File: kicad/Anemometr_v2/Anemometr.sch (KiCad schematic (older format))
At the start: 156 parts, among them J1 TxD, J10 +Z1, J11 +Z2, J12 +Z3, J13 +Z4, J14 -Z1, J15 -Z2, J16 -Z3, J17 -Z4, J18 1 TxD+, J19 2 TxD-, J2 RxD, J20 3 RxD+, J21 4-5, J22 6 RxD-, J23 7-8, J24 Conn_01x01_Female, J3 SCL, J4 SDA, J5 RST, J6 +EXT, J7 -EXT, J8 SWD, J9 SWC, Q1 5N10, U1 STM32F103C8Tx, U2 TS5A3166DBVR, U3 TS5A3166DBVR, U4 TS5A3166DBVR, U5 TS5A3166DBVR, U6 NCP1117-3.3, U7 MCP1703-5, U8 TLV3201DBV, U9 MCP1703-3.3, Y1 CSTCE8M00G52A-R0, Y2 QC5CB25.0000F18B23R

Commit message: изменено:      kicad/Anemometr_v2/Anemometr-cache.lib 	изменено:      kicad/Anemometr_v2/Anemometr.kicad_pcb 	изменено:      kicad/Anemometr_v2/Anemometr.kicad_pcb-bak 	изменено:      kicad/Anemometr_v2/Anemometr.sch 	изменено:      kicad/Anemometr_v2/Anemometr.sch-bak 	изменено:      kicad/Anemometr_v2/fp-info-cache 	изменено:      kicad/Anemometr_v2/gerber/Anemometr-job.gbrjob 	изменено:      kicad/Anemometr_v2/gerber/Border.gbr 	изменено:      kicad/Anemometr_v2/gerber/Bottom.gbr 	изменено:      kicad/Anemometr_v2/gerber/MaskBottom.gbr 	изменено:      kicad/Anemometr_v2/gerber/MaskTop.gbr 	изменено:      kicad/Anemometr_v2/gerber/NCData.drl 	изменено:      kicad/Anemometr_v2/gerber/Top.gbr 	изменено:      kicad/Anemometr_v2/gerber/anemometr.zip
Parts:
- removed Y2: QC5CB25.0000F18B23R, Crystal:Crystal_SMD_Qantek_QC5CB-2Pin_5x3.2mm, symbol Device:Crystal
- added J25: Conn_01x01_Female, My-library:SMD-CONN, symbol Connector:Conn_01x01_Female
- added Y2: ECS-250-20-33, Crystal:Crystal_SMD_SeikoEpson_FA238-4Pin_3.2x2.5mm, symbol Device:Crystal_GND24
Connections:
- net GND: now also Y2.2, Y2.4
- net at C47.2, R37.1, U8.3 (+): now also J25.1 (Pin_1)
- net at C7.1, D3.30 (XI), R1.1: now also Y2.3
- net at C4.1, D3.31 (XO), R1.2: now also Y2.1
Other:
- moved on the sheet: C4, C7, D1, D2, R1, R2, R3
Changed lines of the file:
@@
-$EndComp
-$Comp
-L Device:Crystal Y2
-U 1 1 61F010CD
-P 4550 8250
-F 0 "Y2" H 4200 8350 50  0000 C CNN
-F 1 "QC5CB25.0000F18B23R" H 4200 8250 50  0001 C CNN
-F 2 "Crystal:Crystal_SMD_Qantek_QC5CB-2Pin_5x3.2mm" H 4550 8250 50  0001 C CNN
-F 3 "~" H 4550 8250 50  0001 C CNN
-	1    4550 8250
-	1    0    0    -1
 $EndComp
 $Comp
 L Device:C C4
 U 1 1 61F02281
-P 4400 8400
-F 0 "C4" H 4100 8400 50  0000 L CNN
-F 1 "10p" H 4100 8300 50  0000 L CNN
-F 2 "Capacitor_SMD:C_0402_1005Metric" H 4438 8250 50  0001 C CNN
-F 3 "~" H 4400 8400 50  0001 C CNN
-	1    4400 8400
+P 4150 8600
+F 0 "C4" H 4000 8800 50  0000 L CNN
+F 1 "10p" H 4000 8700 50  0000 L CNN
+F 2 "Capacitor_SMD:C_0402_1005Metric" H 4188 8450 50  0001 C CNN
+F 3 "~" H 4150 8600 50  0001 C CNN
+	1    4150 8600
 	1    0    0    -1
 $EndComp
@@
 L Device:C C7
 U 1 1 61F03145
-P 4700 8400
-F 0 "C7" H 4700 8300 50  0000 L CNN
-F 1 "10p" H 4700 8200 50  0000 L CNN
-F 2 "Capacitor_SMD:C_0402_1005Metric" H 4738 8250 50  0001 C CNN
-F 3 "~" H 4700 8400 50  0001 C CNN
-	1    4700 8400
-	1    0    0    -1
-$EndComp
-Wire Wire Line
-	4400 8550 4550 8550
+P 4450 8600
+F 0 "C7" H 4550 8700 50  0000 L CNN
+F 1 "10p" H 4550 8600 50  0000 L CNN
+F 2 "Capacitor_SMD:C_0402_1005Metric" H 4488 8450 50  0001 C CNN
+F 3 "~" H 4450 8600 50  0001 C CNN
+	1    4450 8600
+	1    0    0    -1
+$EndComp
+Wire Wire Line
+	4150 8750 4300 8750
 $Comp
 L power:GND #PWR04
 U 1 1 61F39844
-P 4550 8550
-F 0 "#PWR04" H 4550 8300 50  0001 C CNN
-F 1 "GND" H 4555 8377 50  0001 C CNN
-F 2 "" H 4550 8550 50  0001 C CNN
-F 3 "" H 4550 8550 50  0001 C CNN
-	1    4550 8550
-	1    0    0    -1
-$EndComp
-Connection ~ 4550 8550
-Wire Wire Line
-	4550 8550 4700 8550
+P 4300 8750
+F 0 "#PWR04" H 4300 8500 50  0001 C CNN
+F 1 "GND" H 4305 8577 50  0001 C CNN
+F 2 "" H 4300 8750 50  0001 C CNN
+F 3 "" H 4300 8750 50  0001 C CNN
+	1    4300 8750
+	1    0    0    -1
+$EndComp
+Connection ~ 4300 8750
+Wire Wire Line
+	4300 8750 4450 8750
 $Comp
 L power:+3.3VA #PWR033
@@
 	-1   0    0    1
 $EndComp
-Wire Wire Line
-	4700 8050 5000 8050
-Wire Wire Line
-	4400 7950 5000 7950
 $Comp
 L Device:C C12
@@
 L Device:LED D1
 U 1 1 62165323
-P 4450 8850
-F 0 "D1" H 4500 8750 50  0000 R CNN
-F 1 "LED" V 4398 8733 50  0001 R CNN
-F 2 "LED_SMD:LED_0603_1608Metric" H 4450 8850 50  0001 C CNN
-F 3 "~" H 4450 8850 50  0001 C CNN
-	1    4450 8850
-	-1   0    0    1
+P 4800 9100
+F 0 "D1" V 4800 9050 50  0000 R CNN
+F 1 "LED" V 4748 8983 50  0001 R CNN
+F 2 "LED_SMD:LED_0603_1608Metric" H 4800 9100 50  0001 C CNN
+F 3 "~" H 4800 9100 50  0001 C CNN
+	1    4800 9100
+	0    1    1    0
 $EndComp
 $Comp
 L Device:LED D2
 U 1 1 62166225
-P 4450 9050
-F 0 "D2" H 4500 9200 50  0000 R CNN
-F 1 "LED" V 4398 8933 50  0001 R CNN
-F 2 "LED_SMD:LED_0603_1608Metric" H 4450 9050 50  0001 C CNN
-F 3 "~" H 4450 9050 50  0001 C CNN
-	1    4450 9050
-	-1   0    0    1
-$EndComp
-Wire Wire Line
-	5000 8350 4900 8350
+P 5000 9100
+F 0 "D2" V 5000 9300 50  0000 R CNN
+F 1 "LED" V 4948 8983 50  0001 R CNN
+F 2 "LED_SMD:LED_0603_1608Metric" H 5000 9100 50  0001 C CNN
+F 3 "~" H 5000 9100 50  0001 C CNN
+	1    5000 9100
+	0    1    1    0
+$EndComp
 $Comp
 L Device:R R2
 U 1 1 6219CE9F
-P 4750 8850
-F 0 "R2" V 4850 8950 50  0000 R CNN
-F 1 "1k" V 4850 8750 50  0000 R CNN
-F 2 "Resistor_SMD:R_0402_1005Metric" V 4680 8850 50  0001 C CNN
-F 3 "~" H 4750 8850 50  0001 C CNN
-	1    4750 8850
-	0    -1   -1   0
+P 4800 8800
+F 0 "R2" H 5050 8800 50  0000 R CNN
+F 1 "1k" H 5050 8900 50  0000 R CNN
+F 2 "Resistor_SMD:R_0402_1005Metric" V 4730 8800 50  0001 C CNN
+F 3 "~" H 4800 8800 50  0001 C CNN
+	1    4800 8800
+	-1   0    0    1
 $EndComp
 $Comp
 L Device:R R3
 U 1 1 6219DA92
-P 4750 9050
-F 0 "R3" V 4650 9150 50  0000 R CNN
-F 1 "1k" V 4650 8950 50  0000 R CNN
-F 2 "Resistor_SMD:R_0402_1005Metric" V 4680 9050 50  0001 C CNN
-F 3 "~" H 4750 9050 50  0001 C CNN
-	1    4750 9050
-	0    -1   -1   0
-$EndComp
-Wire Wire Line
-	4300 8850 4300 9050
+P 5000 8800
+F 0 "R3" H 4900 8900 50  0000 R CNN
+F 1 "1k" H 4900 9000 50  0000 R CNN
+F 2 "Resistor_SMD:R_0402_1005Metric" V 4930 8800 50  0001 C CNN
+F 3 "~" H 5000 8800 50  0001 C CNN
+	1    5000 8800
+	-1   0    0    1
+$EndComp
+Wire Wire Line
+	4800 9250 5000 9250
 NoConn ~ 7000 8550
 NoConn ~ 6550 8950
@@
 Wire Wire Line
 	4450 4650 3900 4650
-Wire Wire Line
-	3900 6950 5450 6950
 NoConn ~ 4450 3850
 NoConn ~ 4450 3950
@@
 Wire Wire Line
 	5800 4250 5750 4250
-Connection ~ 4400 8250
 $Comp
 L Device:R R1
 U 1 1 62826B8F
-P 4550 8050
-F 0 "R1" V 4450 7850 50  0000 R CNN
-F 1 "1M" V 4550 7800 50  0000 R CNN
-F 2 "Resistor_SMD:R_0402_1005Metric" V 4480 8050 50  0001 C CNN
-F 3 "~" H 4550 8050 50  0001 C CNN
-	1    4550 8050
+P 4300 8050
+F 0 "R1" V 4200 7800 50  0000 R CNN
+F 1 "1M" V 4300 7800 50  0000 R CNN
+F 2 "Resistor_SMD:R_0402_1005Metric" V 4230 8050 50  0001 C CNN
+F 3 "~" H 4300 8050 50  0001 C CNN
+	1    4300 8050
 	0    1    1    0
 $EndComp
 Wire Wire Line
-	4400 7950 4400 8050
-Connection ~ 4400 8050
-Wire Wire Line
-	4700 8250 4700 8050
-Connection ~ 4700 8250
-Connection ~ 4700 8050
-Wire Wire Line
-	4400 8050 4400 8250
-Wire Wire Line
-	5000 8550 5000 9050
-Wire Wire Line
-	5000 9050 4900 9050
-Wire Wire Line
-	4900 8350 4900 8850
+	4150 7950 4150 8050
+Connection ~ 4150 8050
+Connection ~ 4450 8050
 $Comp
 L Diode_Bridge:MB6S D12
@@
 L power:+3.3VDAC #PWR03
 U 1 1 6277F4E0
-P 4300 8750
-F 0 "#PWR03" H 4450 8700 50  0001 C CNN
-F 1 "+3.3VDAC" H 4000 8800 50  0000 C CNN
-F 2 "" H 4300 8750 50  0001 C CNN
-F 3 "" H 4300 8750 50  0001 C CNN
-	1    4300 8750
-	1    0    0    -1
+P 4700 9250
+F 0 "#PWR03" H 4850 9200 50  0001 C CNN
+F 1 "+3.3VDAC" V 4750 9500 50  0000 C CNN
+F 2 "" H 4700 9250 50  0001 C CNN
+F 3 "" H 4700 9250 50  0001 C CNN
+	1    4700 9250
+	0    -1   -1   0
 $EndComp
 $Comp
@@
 	0    1    1    0
 $EndComp
-Connection ~ 4300 8850
+Connection ~ 4800 9250
 $Comp
 L power:+3.3VDAC #PWR08
@@
 U 1 1 61F1031D
 P 7950 8400
-F 0 "R14" H 7750 8600 50  0000 R CNN
-F 1 "82R" H 7750 8700 50  0000 R CNN
+F 0 "R14" H 7850 8400 50  0000 R CNN
+F 1 "82R" H 7850 8500 50  0000 R CNN
 F 2 "Resistor_SMD:R_0402_1005Metric" V 7880 8400 50  0001 C CNN
 F 3 "~" H 7950 8400 50  0001 C CNN
@@
 U 1 1 61F1100A
 P 7950 8700
-F 0 "C16" H 8150 8650 50  0000 L CNN
-F 1 "10nF" H 8100 8750 50  0000 L CNN
+F 0 "C16" H 7700 8650 50  0000 L CNN
+F 1 "10nF" H 7650 8750 50  0000 L CNN
 F 2 "Capacitor_SMD:C_0402_1005Metric" H 7988 8550 50  0001 C CNN
 F 3 "~" H 7950 8700 50  0001 C CNN
@@
 	4150 5450 4150 7850
 Wire Wire Line
-	3900 4650 3900 6950
+	3900 4650 3900 6800
 NoConn ~ 5000 7450
 NoConn ~ 4450 4550
@@
 U 1 1 61F0FDA5
 P 8150 8200
-F 0 "C26" V 8000 8100 50  0000 L CNN
-F 1 "6.8nF" V 7900 8050 50  0000 L CNN
+F 0 "C26" V 8300 7950 50  0000 L CNN
+F 1 "6.8nF" V 8200 7900 50  0000 L CNN
 F 2 "Capacitor_SMD:C_0402_1005Metric" H 8188 8050 50  0001 C CNN
 F 3 "~" H 8150 8200 50  0001 C CNN
@@
 	6150 6850 6150 6950
 Wire Wire Line
-	4300 8750 4300 8850
+	4700 9250 4800 9250
 Wire Wire Line
 	7100 9050 7100 9150
@@
 Connection ~ 11400 7850
 Wire Wire Line
-	10400 7450 10400 7650
-Wire Wire Line
-	10400 7450 11750 7450
-Wire Wire Line
-	9600 7650 10400 7650
-Wire Wire Line
 	10600 6700 10600 7500
 Wire Wire Line
@@
 Wire Wire Line
 	10600 7500 10600 7950
+Wire Wire Line
+	5450 6950 5450 6800
+Wire Wire Line
+	5450 6800 3900 6800
+Wire Wire Line
+	10700 7650 10700 7450
+Wire Wire Line
+	10700 7450 11750 7450
+Wire Wire Line
+	9600 7650 10700 7650
+$Comp
+L Device:Crystal_GND24 Y2
+U 1 1 629362D8
+P 4300 8350
+F 0 "Y2" H 4494 8350 50  0000 L CNN
+F 1 "ECS-250-20-33" H 4494 8305 50  0001 L CNN
+F 2 "Crystal:Crystal_SMD_SeikoEpson_FA238-4Pin_3.2x2.5mm" H 4300 8350 50  0001 C CNN
+F 3 "~" H 4300 8350 50  0001 C CNN
+	1    4300 8350
+	1    0    0    -1
+$EndComp
+Wire Wire Line
+	4450 8050 4450 8350
+Connection ~ 4450 8350
+Wire Wire Line
+	4450 8350 4450 8450
+Wire Wire Line
+	4150 8050 4150 8350
+Connection ~ 4150 8350
+Wire Wire Line
+	4150 8350 4150 8450
+Wire Wire Line
+	4150 7950 5000 7950
+Wire Wire Line
+	4450 8050 5000 8050
+Wire Wire Line
+	5000 8550 5000 8650
+Wire Wire Line
+	4800 8350 4800 8650
+Wire Wire Line
+	4800 8350 5000 8350
+Wire Wire Line
+	4300 8550 4300 8750
+Wire Wire Line
+	4300 8150 3950 8150
+Wire Wire Line
+	3950 8150 3950 8750
+Wire Wire Line
+	3950 8750 4150 8750
+Connection ~ 4150 8750
+$Comp
+L Connector:Conn_01x01_Female J25
+U 1 1 62BD7268
+P 11100 1900
+F 0 "J25" H 11128 1880 50  0001 L CNN
+F 1 "Conn_01x01_Female" H 11128 1835 50  0001 L CNN
+F 2 "My-library:SMD-CONN" H 11100 1900 50  0001 C CNN
+F 3 "~" H 11100 1900 50  0001 C CNN
+	1    11100 1900
+	0    -1   -1   0
+$EndComp
 $EndSCHEMATC

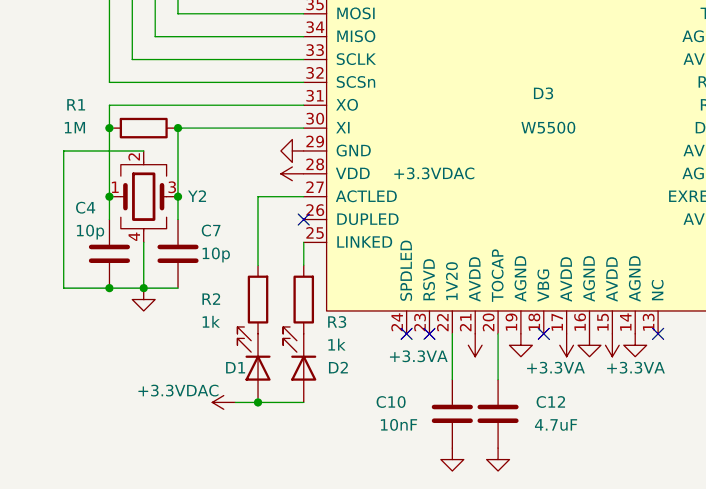
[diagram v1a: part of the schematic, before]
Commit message: изменено:      kicad/Anemometr_v2/Anemometr-cache.lib 	изменено:      kicad/Anemometr_v2/Anemometr.sch 	изменено:      kicad/Anemometr_v2/Anemometr.sch-bak 	изменено:      kicad/Anemometr_v2/bom/ibom.html
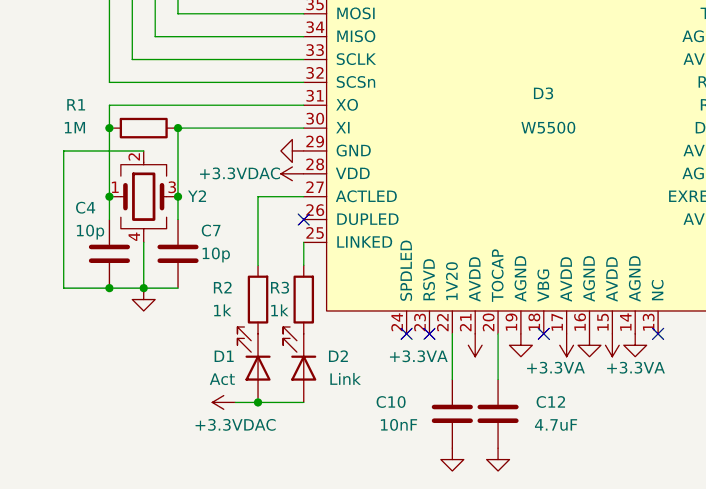
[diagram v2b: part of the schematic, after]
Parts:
- D1: value LED -> Act
- D2: value LED -> Link
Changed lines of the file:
@@
 U 1 1 62165323
 P 4800 9100
-F 0 "D1" V 4800 9050 50  0000 R CNN
-F 1 "LED" V 4748 8983 50  0001 R CNN
+F 0 "D1" V 4750 9000 50  0000 R CNN
+F 1 "Act" V 4850 9000 50  0000 R CNN
 F 2 "LED_SMD:LED_0603_1608Metric" H 4800 9100 50  0001 C CNN
 F 3 "~" H 4800 9100 50  0001 C CNN
@@
 U 1 1 62166225
 P 5000 9100
-F 0 "D2" V 5000 9300 50  0000 R CNN
-F 1 "LED" V 4948 8983 50  0001 R CNN
+F 0 "D2" V 4950 9300 50  0000 R CNN
+F 1 "Link" V 5050 9350 50  0000 R CNN
 F 2 "LED_SMD:LED_0603_1608Metric" H 5000 9100 50  0001 C CNN
 F 3 "~" H 5000 9100 50  0001 C CNN
@@
 U 1 1 6219CE9F
 P 4800 8800
-F 0 "R2" H 5050 8800 50  0000 R CNN
-F 1 "1k" H 5050 8900 50  0000 R CNN
+F 0 "R2" H 5000 8750 50  0000 R CNN
+F 1 "1k" H 5000 8850 50  0000 R CNN
 F 2 "Resistor_SMD:R_0402_1005Metric" V 4730 8800 50  0001 C CNN
 F 3 "~" H 4800 8800 50  0001 C CNN
@@
 U 1 1 6219DA92
 P 5000 8800
-F 0 "R3" H 4900 8900 50  0000 R CNN
-F 1 "1k" H 4900 9000 50  0000 R CNN
+F 0 "R3" H 5150 8750 50  0000 R CNN
+F 1 "1k" H 5150 8850 50  0000 R CNN
 F 2 "Resistor_SMD:R_0402_1005Metric" V 4930 8800 50  0001 C CNN
 F 3 "~" H 5000 8800 50  0001 C CNN
@@
 P 4700 9250
 F 0 "#PWR03" H 4850 9200 50  0001 C CNN
-F 1 "+3.3VDAC" V 4750 9500 50  0000 C CNN
+F 1 "+3.3VDAC" V 4600 9250 50  0000 C CNN
 F 2 "" H 4700 9250 50  0001 C CNN
 F 3 "" H 4700 9250 50  0001 C CNN
@@
 P 5000 8250
 F 0 "#PWR08" H 5150 8200 50  0001 C CNN
-F 1 "+3.3VDAC" V 5000 7500 50  0000 L CNN
+F 1 "+3.3VDAC" V 5000 8350 50  0000 L CNN
 F 2 "" H 5000 8250 50  0001 C CNN
 F 3 "" H 5000 8250 50  0001 C CNN

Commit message: изменено:      kicad/Anemometr_v2/Anemometr-cache.lib 	изменено:      kicad/Anemometr_v2/Anemometr.kicad_pcb 	изменено:      kicad/Anemometr_v2/Anemometr.kicad_pcb-bak 	изменено:      kicad/Anemometr_v2/Anemometr.sch 	изменено:      kicad/Anemometr_v2/Anemometr.sch-bak
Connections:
- net Analog: now reaches C47.2, J25.1 (Pin_1), R37.1, U8.3 (+)
- net Analog: now also U1.18 (PB0)
- no-connect marks 29 -> 28
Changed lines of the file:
@@
 NoConn ~ 4450 3950
 NoConn ~ 4450 4050
-NoConn ~ 4450 4250
 NoConn ~ 4450 4750
-NoConn ~ 5750 4350
 NoConn ~ 5750 4450
 NoConn ~ 5750 4550
@@
 	0    -1   -1   0
 $EndComp
+Text GLabel 10950 2300 0    50   Input ~ 0
+Analog
+Wire Wire Line
+	10950 2300 11100 2300
+Connection ~ 11100 2300
+Text GLabel 4450 4250 0    50   Input ~ 0
+Analog
+NoConn ~ 5750 4350
 $EndSCHEMATC

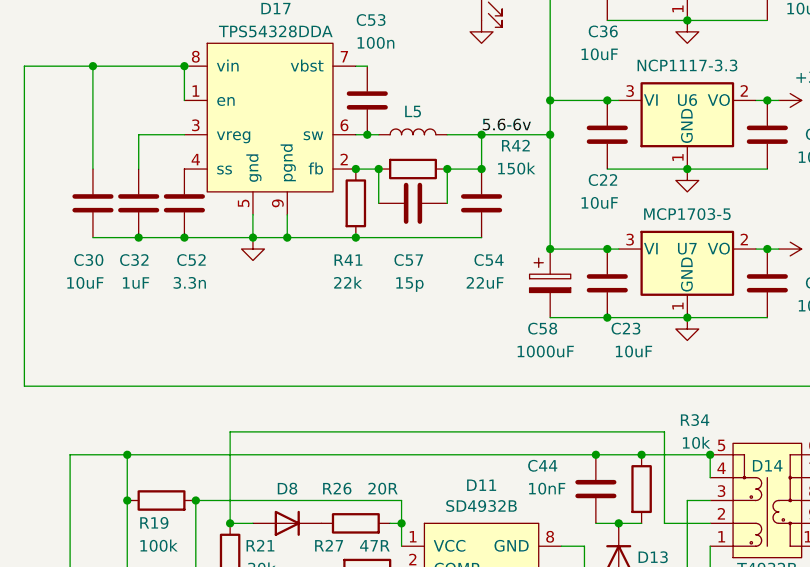
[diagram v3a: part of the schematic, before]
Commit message: изменено:      kicad/Anemometr_v2/Anemometr.sch 	изменено:      kicad/Anemometr_v2/Anemometr.sch-bak 	изменено:      stm32cubeide/Anemometer/Anemometer.ioc 	изменено:      stm32cubeide/Anemometer/Core/Inc/stm32f1xx_hal_conf.h 	изменено:      stm32cubeide/Anemometer/Core/Src/main.c 	изменено:      stm32cubeide/Anemometer/Core/Src/stm32f1xx_hal_msp.c 	изменено:      stm32cubeide/Anemometer/Core/Src/stm32f1xx_it.c 	изменено:      stm32cubeide/Anemometer/Release/Anemometer.bin 	изменено:      stm32cubeide/Anemometer/Release/Anemometer.elf 	изменено:      stm32cubeide/Anemometer/Release/Anemometer.list 	изменено:      stm32cubeide/Anemometer/Release/Anemometer.map 	изменено:      stm32cubeide/Anemometer/Release/Core/Src/main.o 	изменено:      stm32cubeide/Anemometer/Release/Core/Src/main.su 	изменено:      stm32cubeide/Anemometer/Release/Core/Src/stm32f1xx_hal_msp.o 	изменено:      stm32cubeide/Anemometer/Release/Core/Src/stm32f1xx_hal_msp.su 	изменено:      stm32cubeide/Anemometer/Release/Core/Src/stm32f1xx_it.o 	изменено:      stm32cubeide/Anemometer/Release/Core/Src/stm32f1xx_it.su 	изменено:      stm32cubeide/Anemometer/Release/Core/Src/system_stm32f1xx.o 	изменено:      stm32cubeide/Anemometer/Release/Drivers/STM32F1xx_HAL_Driver/Src/stm32f1xx_hal_rcc.o 	изменено:      stm32cubeide/Anemometer/Release/Drivers/STM32F1xx_HAL_Driver/Src/stm32f1xx_hal_rcc_ex.o
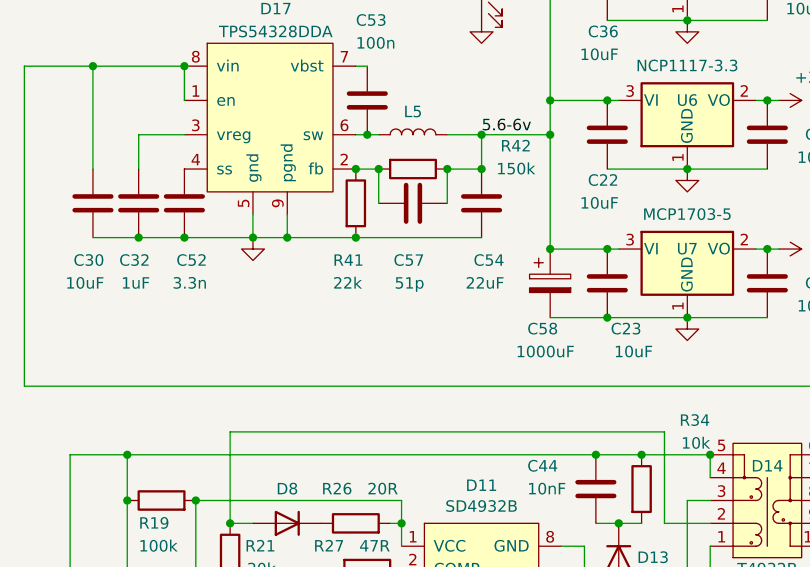
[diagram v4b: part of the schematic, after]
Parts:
- C57: value 15p -> 51p
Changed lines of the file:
@@
 P 9550 4100
 F 0 "C57" V 9300 4050 50  0000 L CNN
-F 1 "15p" V 9200 4050 50  0000 L CNN
+F 1 "51p" V 9200 4050 50  0000 L CNN
 F 2 "Capacitor_SMD:C_0603_1608Metric" H 9588 3950 50  0001 C CNN
 F 3 "~" H 9550 4100 50  0001 C CNN
